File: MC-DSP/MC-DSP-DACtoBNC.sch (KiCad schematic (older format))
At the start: 1 part

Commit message: ADC refs, FTDI changes, and more
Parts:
- removed J?: Conn_Coaxial, symbol Connector:Conn_Coaxial
- added C? (x3): 0.1uF, symbol Device:C
- added J?: CONMMCX001, LINX_CONMMCX001, symbol CONMMCX001:CONMMCX001
- added R? (x2): ?R, symbol Device:R
- added R?: 0R, symbol Device:R
- added U?: OPA365xxD, Package_SO:SOIC-8_3.9x4.9mm_P1.27mm, symbol Amplifier_Operational:OPA365xxD
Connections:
- net labels added: DAC_A, DAC_B, DAC_C, VDDA
- net labels removed: DACfromDSP
- wire segments 1 -> 17
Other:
- note added: "check datasheet to pick between VDDA (3.3V) or VDAC (3V)"
- note added: "note offset error of 1-15 mV\n"
- note added: "read Output Capacitive Loading and Stability\n, add pads for an input resistor"
- note added: "verify input range\n"
- note removed: "Look for line driver amplifiers (look at appnotes)"
- note removed: "switch to mmcx"
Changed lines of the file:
@@
 $Descr A4 11693 8268
 encoding utf-8
-Sheet 9 9
+Sheet 7 9
 Title ""
 Date ""
@@
 Comment4 ""
 $EndDescr
-$Comp
-L Connector:Conn_Coaxial J?
-U 1 1 61B9DADA
-P 7400 2700
-F 0 "J?" H 7500 2675 50  0000 L CNN
-F 1 "Conn_Coaxial" H 7500 2584 50  0000 L CNN
-F 2 "" H 7400 2700 50  0001 C CNN
-F 3 " ~" H 7400 2700 50  0001 C CNN
-	1    7400 2700
-	1    0    0    -1
-$EndComp
-Text HLabel 4450 2650 0    50   Input ~ 0
-DACfromDSP
+Text HLabel 4600 2850 0    50   Input ~ 0
+DAC_A
 $Comp
 L power:GND #PWR?
 U 1 1 61B9E54E
-P 7400 3150
-F 0 "#PWR?" H 7400 2900 50  0001 C CNN
-F 1 "GND" H 7405 2977 50  0000 C CNN
-F 2 "" H 7400 3150 50  0001 C CNN
-F 3 "" H 7400 3150 50  0001 C CNN
-	1    7400 3150
-	1    0    0    -1
-$EndComp
-Wire Wire Line
-	7400 3150 7400 2900
-Text Notes 4950 2400 0    50   ~ 0
-Look for line driver amplifiers (look at appnotes)
-Text Notes 7450 2450 0    50   ~ 0
-switch to mmcx
+P 7350 3300
+F 0 "#PWR?" H 7350 3050 50  0001 C CNN
+F 1 "GND" H 7355 3127 50  0000 C CNN
+F 2 "" H 7350 3300 50  0001 C CNN
+F 3 "" H 7350 3300 50  0001 C CNN
+	1    7350 3300
+	1    0    0    -1
+$EndComp
+Wire Wire Line
+	7350 3300 7350 3050
+Wire Wire Line
+	6250 2950 6350 2950
+Wire Wire Line
+	5650 2850 5300 2850
+$Comp
+L CONMMCX001:CONMMCX001 J?
+U 1 1 61F03ABB
+P 7450 3050
+F 0 "J?" H 7296 3136 50  0000 R CNN
+F 1 "CONMMCX001" H 7296 3045 50  0000 R CNN
+F 2 "LINX_CONMMCX001" H 7450 3050 50  0001 L BNN
+F 3 "" H 7450 3050 50  0001 L BNN
+F 4 "B" H 7450 3050 50  0001 L BNN "PARTREV"
+F 5 "Manufacturer Recommendations" H 7450 3050 50  0001 L BNN "STANDARD"
+F 6 "Linx Technologies" H 7450 3050 50  0001 L BNN "MANUFACTURER"
+	1    7450 3050
+	-1   0    0    -1
+$EndComp
+Text HLabel 4450 3900 0    50   Input ~ 0
+DAC_B
+Text HLabel 4450 4750 0    50   Input ~ 0
+DAC_C
+Text Notes 6500 1100 0    50   ~ 0
+verify input range\n
+Text Notes 6400 1200 0    50   ~ 0
+note offset error of 1-15 mV\n
+Text Notes 7550 1050 0    50   ~ 0
+read Output Capacitive Loading and Stability\n, add pads for an input resistor
+$Comp
+L Amplifier_Operational:OPA365xxD U?
+U 1 1 622D9ECC
+P 5950 2950
+F 0 "U?" H 5950 3200 50  0000 L CNN
+F 1 "OPA365xxD" H 5950 3100 50  0000 L CNN
+F 2 "Package_SO:SOIC-8_3.9x4.9mm_P1.27mm" H 5850 2750 50  0001 L CNN
+F 3 "http://www.ti.com/lit/ds/symlink/opa365.pdf" H 6100 3100 50  0001 C CNN
+	1    5950 2950
+	1    0    0    -1
+$EndComp
+$Comp
+L power:GND #PWR?
+U 1 1 62433A6D
+P 3950 2050
+AR Path="/62086B6E/62433A6D" Ref="#PWR?"  Part="1"
+AR Path="/61B9C0F2/62433A6D" Ref="#PWR?"  Part="1"
+F 0 "#PWR?" H 3950 1800 50  0001 C CNN
+F 1 "GND" H 3955 1877 50  0000 C CNN
+F 2 "" H 3950 2050 50  0001 C CNN
+F 3 "" H 3950 2050 50  0001 C CNN
+	1    3950 2050
+	1    0    0    -1
+$EndComp
+$Comp
+L Device:C C?
+U 1 1 62433A73
+P 3800 1900
+F 0 "C?" H 3750 1800 50  0000 R CNN
+F 1 "0.1uF" H 3750 2000 50  0000 R CNN
+F 2 "" H 3838 1750 50  0001 C CNN
+F 3 "~" H 3800 1900 50  0001 C CNN
+	1    3800 1900
+	-1   0    0    1
+$EndComp
+$Comp
+L power:VDDA #PWR?
+U 1 1 62433A79
+P 3950 1750
+AR Path="/62086B6E/62433A79" Ref="#PWR?"  Part="1"
+AR Path="/61B9C0F2/62433A79" Ref="#PWR?"  Part="1"
+F 0 "#PWR?" H 3950 1600 50  0001 C CNN
+F 1 "VDDA" H 3965 1923 50  0000 C CNN
+F 2 "" H 3950 1750 50  0001 C CNN
+F 3 "" H 3950 1750 50  0001 C CNN
+	1    3950 1750
+	1    0    0    -1
+$EndComp
+$Comp
+L Device:C C?
+U 1 1 62433A7F
+P 4100 1900
+F 0 "C?" H 4050 1800 50  0000 R CNN
+F 1 "0.1uF" H 4050 2000 50  0000 R CNN
+F 2 "" H 4138 1750 50  0001 C CNN
+F 3 "~" H 4100 1900 50  0001 C CNN
+	1    4100 1900
+	-1   0    0    1
+$EndComp
+$Comp
+L Device:C C?
+U 1 1 62433A85
+P 4400 1900
+F 0 "C?" H 4350 1800 50  0000 R CNN
+F 1 "0.1uF" H 4350 2000 50  0000 R CNN
+F 2 "" H 4438 1750 50  0001 C CNN
+F 3 "~" H 4400 1900 50  0001 C CNN
+	1    4400 1900
+	-1   0    0    1
+$EndComp
+Wire Wire Line
+	3950 1750 3800 1750
+Connection ~ 4100 1750
+Wire Wire Line
+	4100 1750 4400 1750
+Wire Wire Line
+	3800 2050 3950 2050
+Connection ~ 4100 2050
+Wire Wire Line
+	4100 2050 4400 2050
+Connection ~ 3950 1750
+Wire Wire Line
+	3950 1750 4100 1750
+Connection ~ 3950 2050
+Wire Wire Line
+	3950 2050 4100 2050
+$Comp
+L power:VDDA #PWR?
+U 1 1 624345BF
+P 5850 2650
+AR Path="/62086B6E/624345BF" Ref="#PWR?"  Part="1"
+AR Path="/61B9C0F2/624345BF" Ref="#PWR?"  Part="1"
+F 0 "#PWR?" H 5850 2500 50  0001 C CNN
+F 1 "VDDA" H 6000 2700 50  0000 C CNN
+F 2 "" H 5850 2650 50  0001 C CNN
+F 3 "" H 5850 2650 50  0001 C CNN
+	1    5850 2650
+	1    0    0    -1
+$EndComp
+$Comp
+L power:GND #PWR?
+U 1 1 6243580E
+P 5850 3250
+AR Path="/62086B6E/6243580E" Ref="#PWR?"  Part="1"
+AR Path="/61B9C0F2/6243580E" Ref="#PWR?"  Part="1"
+F 0 "#PWR?" H 5850 3000 50  0001 C CNN
+F 1 "GND" H 6000 3200 50  0000 C CNN
+F 2 "" H 5850 3250 50  0001 C CNN
+F 3 "" H 5850 3250 50  0001 C CNN
+	1    5850 3250
+	1    0    0    -1
+$EndComp
+Wire Wire Line
+	5650 3050 5550 3050
+Wire Wire Line
+	5550 3050 5550 3450
+Wire Wire Line
+	5550 3450 5750 3450
+Wire Wire Line
+	6350 3450 6350 2950
+Connection ~ 6350 2950
+Wire Wire Line
+	6350 2950 6700 2950
+$Comp
+L Device:R R?
+U 1 1 62439A67
+P 6850 2950
+F 0 "R?" V 6850 2950 50  0000 C CNN
+F 1 "?R" V 6734 2950 50  0000 C CNN
+F 2 "" V 6780 2950 50  0001 C CNN
+F 3 "~" H 6850 2950 50  0001 C CNN
+	1    6850 2950
+	0    1    1    0
+$EndComp
+Wire Wire Line
+	7000 2950 7350 2950
+$Comp
+L Device:R R?
+U 1 1 6243BA69
+P 5150 2850
+F 0 "R?" V 5150 2850 50  0000 C CNN
+F 1 "0R" V 5034 2850 50  0000 C CNN
+F 2 "" V 5080 2850 50  0001 C CNN
+F 3 "~" H 5150 2850 50  0001 C CNN
+	1    5150 2850
+	0    1    1    0
+$EndComp
+Wire Wire Line
+	5000 2850 4600 2850
+$Comp
+L Device:R R?
+U 1 1 6243CB15
+P 5900 3450
+F 0 "R?" V 5900 3450 50  0000 C CNN
+F 1 "?R" V 6000 3450 50  0000 C CNN
+F 2 "" V 5830 3450 50  0001 C CNN
+F 3 "~" H 5900 3450 50  0001 C CNN
+	1    5900 3450
+	0    1    1    0
+$EndComp
+Wire Wire Line
+	6050 3450 6350 3450
+Text Notes 5600 2450 0    50   ~ 0
+check datasheet to pick between VDDA (3.3V) or VDAC (3V)
 $EndSCHEMATC

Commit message: fixed some dsp pin routing
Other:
- note removed: "check datasheet to pick between VDDA (3.3V) or VDAC (3V)"
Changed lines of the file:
@@
 Wire Wire Line
 	6050 3450 6350 3450
-Text Notes 5600 2450 0    50   ~ 0
-check datasheet to pick between VDDA (3.3V) or VDAC (3V)
 $EndSCHEMATC

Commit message: All parts labeled, just need to pick passives basically.
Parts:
- removed J?: CONMMCX001, LINX_CONMMCX001, symbol CONMMCX001:CONMMCX001
- added J60, J61, J62: Conn_Coaxial, ?, symbol Connector:Conn_Coaxial
- added R61, R62: 10R, Resistor_SMD:R_0603_1608Metric_Pad0.98x0.95mm_HandSolder, symbol Device:R
- added R64, R65, R67, R68: 0R, Resistor_SMD:R_0603_1608Metric_Pad0.98x0.95mm_HandSolder, symbol Device:R
- added U61, U62: OPA365xxD, Package_SO:SOIC-8_3.9x4.9mm_P1.27mm, symbol Amplifier_Operational:OPA365xxD
- C60, C61, C62: renamed from C?; footprint (none) -> Capacitor_SMD:C_0201_0603Metric_Pad0.64x0.40mm_HandSolder
- R60: renamed from R?; value ?R -> 10R; footprint (none) -> Resistor_SMD:R_0603_1608Metric_Pad0.98x0.95mm_HandSolder
- R63: renamed from R?; value ?R -> 0R; footprint (none) -> Resistor_SMD:R_0603_1608Metric_Pad0.98x0.95mm_HandSolder
- R66: renamed from R?; footprint (none) -> Resistor_SMD:R_0603_1608Metric_Pad0.98x0.95mm_HandSolder
- gave numbers to parts that had none: 1
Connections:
- wire segments 17 -> 39
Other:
- note removed: "note offset error of 1-15 mV\n"
- note removed: "read Output Capacitive Loading and Stability\n, add pads for an input resistor"
- note removed: "verify input range\n"
- moved on the sheet: C60, C61, C62

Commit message: DSP - added footprints and links to most parts
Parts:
- removed J60, J61, J62: Conn_Coaxial, ?, symbol Connector:Conn_Coaxial
- added J80, J81, J82: 5-1634513-1, 516345131, symbol 5-1634513-1:5-1634513-1
- renumbered C60 to C80, C61 to C81, C62 to C82, R60 to R80, R61 to R81, R62 to R82, R63 to R83, R64 to R84, R65 to R85, R66 to R86, R67 to R87, R68 to R88, U60 to U80, U61 to U81, U62 to U82
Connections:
- wire segments 39 -> 54

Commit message: Removed clock buffer, misc leds, ethernet
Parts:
- C80, C81, C82: footprint Capacitor_SMD:C_0201_0603Metric_Pad0.64x0.40mm_HandSolder -> Capacitor_SMD:C_0603_1608Metric_Pad1.08x0.95mm_HandSolder
- J80, J81, J82: footprint 516345131 -> mark_footprints:516345131
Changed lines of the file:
@@
 $Descr A4 11693 8268
 encoding utf-8
-Sheet 7 9
+Sheet 7 7
 Title ""
 Date ""
@@
 F 0 "C80" H 4600 1850 50  0000 R CNN
 F 1 "0.1uF" H 4600 2050 50  0000 R CNN
-F 2 "Capacitor_SMD:C_0201_0603Metric_Pad0.64x0.40mm_HandSolder" H 4688 1800 50  0001 C CNN
+F 2 "Capacitor_SMD:C_0603_1608Metric_Pad1.08x0.95mm_HandSolder" H 4688 1800 50  0001 C CNN
 F 3 "https://www.digikey.com/en/products/detail/yageo/CC0603KRX7R9BB104/2103082" H 4650 1950 50  0001 C CNN
 	1    4650 1950
@@
 F 0 "C81" H 4900 1850 50  0000 R CNN
 F 1 "0.1uF" H 4900 2050 50  0000 R CNN
-F 2 "Capacitor_SMD:C_0201_0603Metric_Pad0.64x0.40mm_HandSolder" H 4988 1800 50  0001 C CNN
+F 2 "Capacitor_SMD:C_0603_1608Metric_Pad1.08x0.95mm_HandSolder" H 4988 1800 50  0001 C CNN
 F 3 "https://www.digikey.com/en/products/detail/yageo/CC0603KRX7R9BB104/2103082" H 4950 1950 50  0001 C CNN
 	1    4950 1950
@@
 F 0 "C82" H 5200 1850 50  0000 R CNN
 F 1 "0.1uF" H 5200 2050 50  0000 R CNN
-F 2 "Capacitor_SMD:C_0201_0603Metric_Pad0.64x0.40mm_HandSolder" H 5288 1800 50  0001 C CNN
+F 2 "Capacitor_SMD:C_0603_1608Metric_Pad1.08x0.95mm_HandSolder" H 5288 1800 50  0001 C CNN
 F 3 "https://www.digikey.com/en/products/detail/yageo/CC0603KRX7R9BB104/2103082" H 5250 1950 50  0001 C CNN
 	1    5250 1950
@@
 F 0 "J80" H 7750 3215 50  0000 C CNN
 F 1 "5-1634513-1" H 7750 3124 50  0000 C CNN
-F 2 "516345131" H 8000 3050 50  0001 L CNN
+F 2 "mark_footprints:516345131" H 8000 3050 50  0001 L CNN
 F 3 "https://www.digikey.com/en/products/detail/te-connectivity-amp-connectors/5-1634513-1/1755956?s=N4IgTCBcDaIKwFoCMA2AzAFjktyQF0BfIA" H 8000 2950 50  0001 L CNN
 F 4 "Connector,Coaxial,BNC,PCB,Socket,R/A,Elbow,50Ohm,Nickel Plated,28.0mm" H 8000 2850 50  0001 L CNN "Description"
@@
 F 0 "J81" H 7750 4515 50  0000 C CNN
 F 1 "5-1634513-1" H 7750 4424 50  0000 C CNN
-F 2 "516345131" H 8000 4350 50  0001 L CNN
+F 2 "mark_footprints:516345131" H 8000 4350 50  0001 L CNN
 F 3 "https://www.digikey.com/en/products/detail/te-connectivity-amp-connectors/5-1634513-1/1755956?s=N4IgTCBcDaIKwFoCMA2AzAFjktyQF0BfIA" H 8000 4250 50  0001 L CNN
 F 4 "Connector,Coaxial,BNC,PCB,Socket,R/A,Elbow,50Ohm,Nickel Plated,28.0mm" H 8000 4150 50  0001 L CNN "Description"
@@
 F 0 "J82" H 7750 5715 50  0000 C CNN
 F 1 "5-1634513-1" H 7750 5624 50  0000 C CNN
-F 2 "516345131" H 8000 5550 50  0001 L CNN
+F 2 "mark_footprints:516345131" H 8000 5550 50  0001 L CNN
 F 3 "https://www.digikey.com/en/products/detail/te-connectivity-amp-connectors/5-1634513-1/1755956?s=N4IgTCBcDaIKwFoCMA2AzAFjktyQF0BfIA" H 8000 5450 50  0001 L CNN
 F 4 "Connector,Coaxial,BNC,PCB,Socket,R/A,Elbow,50Ohm,Nickel Plated,28.0mm" H 8000 5350 50  0001 L CNN "Description"

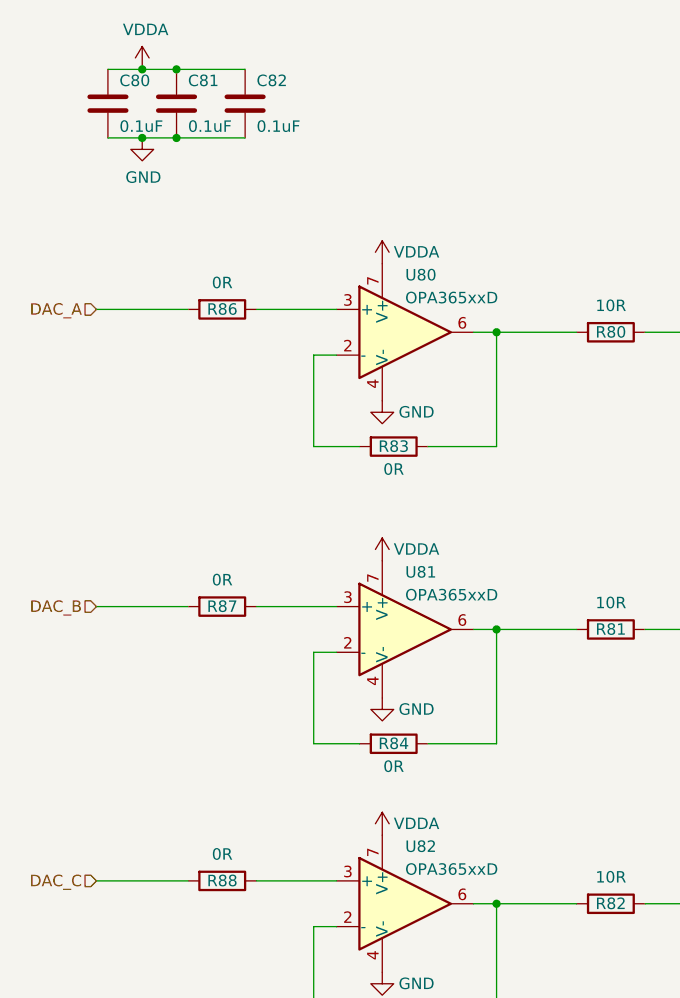
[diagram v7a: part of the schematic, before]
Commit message: Total overhaul of power planes. Routed whole Analog section, middle of digital section.
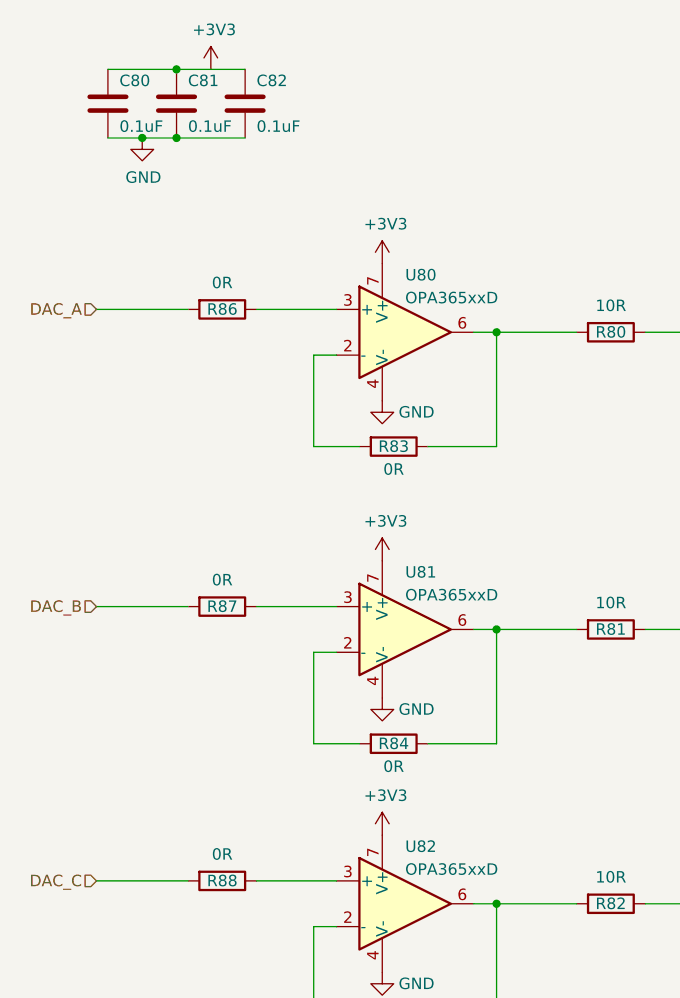
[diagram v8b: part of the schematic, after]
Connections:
- net VDDA: no longer names the net of C80.2, C81.2, C82.2
- net VDDA: no longer U80.7 (V+), U81.7 (V+), U82.7 (V+)
- new net +3V3: U80.7 (V+), U81.7 (V+), U82.7 (V+)
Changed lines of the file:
@@
 $Descr A4 11693 8268
 encoding utf-8
-Sheet 4 7
+Sheet 2 7
 Title ""
 Date ""
@@
 $EndComp
 $Comp
-L power:VDDA #PWR?
-U 1 1 62433A79
-P 4800 1800
-AR Path="/62086B6E/62433A79" Ref="#PWR?"  Part="1"
-AR Path="/61B9C0F2/62433A79" Ref="#PWR0173"  Part="1"
-F 0 "#PWR0173" H 4800 1650 50  0001 C CNN
-F 1 "VDDA" H 4815 1973 50  0000 C CNN
-F 2 "" H 4800 1800 50  0001 C CNN
-F 3 "" H 4800 1800 50  0001 C CNN
-	1    4800 1800
-	1    0    0    -1
-$EndComp
-$Comp
 L Device:C C81
 U 1 1 62433A7F
@@
 	-1   0    0    1
 $EndComp
-Wire Wire Line
-	4800 1800 4650 1800
 Connection ~ 4950 1800
 Wire Wire Line
@@
 Wire Wire Line
 	4950 2100 5250 2100
-Connection ~ 4800 1800
-Wire Wire Line
-	4800 1800 4950 1800
 Connection ~ 4800 2100
 Wire Wire Line
 	4800 2100 4950 2100
-$Comp
-L power:VDDA #PWR?
-U 1 1 624345BF
-P 5850 2650
-AR Path="/62086B6E/624345BF" Ref="#PWR?"  Part="1"
-AR Path="/61B9C0F2/624345BF" Ref="#PWR0174"  Part="1"
-F 0 "#PWR0174" H 5850 2500 50  0001 C CNN
-F 1 "VDDA" H 6000 2700 50  0000 C CNN
-F 2 "" H 5850 2650 50  0001 C CNN
-F 3 "" H 5850 2650 50  0001 C CNN
-	1    5850 2650
-	1    0    0    -1
-$EndComp
 $Comp
 L power:GND #PWR?
@@
 $EndComp
 $Comp
-L power:VDDA #PWR?
-U 1 1 6337731D
-P 5850 3950
-AR Path="/62086B6E/6337731D" Ref="#PWR?"  Part="1"
-AR Path="/61B9C0F2/6337731D" Ref="#PWR0176"  Part="1"
-F 0 "#PWR0176" H 5850 3800 50  0001 C CNN
-F 1 "VDDA" H 6000 4000 50  0000 C CNN
-F 2 "" H 5850 3950 50  0001 C CNN
-F 3 "" H 5850 3950 50  0001 C CNN
-	1    5850 3950
-	1    0    0    -1
-$EndComp
-$Comp
 L power:GND #PWR?
 U 1 1 63377323
@@
 F 3 "https://www.digikey.com/en/products/detail/texas-instruments/OPA365AID/1219893" H 6100 5600 50  0001 C CNN
 	1    5950 5450
-	1    0    0    -1
-$EndComp
-$Comp
-L power:VDDA #PWR?
-U 1 1 6337C61B
-P 5850 5150
-AR Path="/62086B6E/6337C61B" Ref="#PWR?"  Part="1"
-AR Path="/61B9C0F2/6337C61B" Ref="#PWR0178"  Part="1"
-F 0 "#PWR0178" H 5850 5000 50  0001 C CNN
-F 1 "VDDA" H 6000 5200 50  0000 C CNN
-F 2 "" H 5850 5150 50  0001 C CNN
-F 3 "" H 5850 5150 50  0001 C CNN
-	1    5850 5150
 	1    0    0    -1
 $EndComp
@@
 Wire Wire Line
 	7350 4250 7000 4250
+$Comp
+L power:+3V3 #PWR?
+U 1 1 6242ED79
+P 5850 3950
+AR Path="/6187F723/6242ED79" Ref="#PWR?"  Part="1"
+AR Path="/61B9C0F2/6242ED79" Ref="#PWR0139"  Part="1"
+F 0 "#PWR0139" H 5850 3800 50  0001 C CNN
+F 1 "+3V3" H 5865 4123 50  0000 C CNN
+F 2 "" H 5850 3950 50  0001 C CNN
+F 3 "" H 5850 3950 50  0001 C CNN
+	1    5850 3950
+	1    0    0    -1
+$EndComp
+$Comp
+L power:+3V3 #PWR?
+U 1 1 62430BBE
+P 5850 2650
+AR Path="/6187F723/62430BBE" Ref="#PWR?"  Part="1"
+AR Path="/61B9C0F2/62430BBE" Ref="#PWR0140"  Part="1"
+F 0 "#PWR0140" H 5850 2500 50  0001 C CNN
+F 1 "+3V3" H 5865 2823 50  0000 C CNN
+F 2 "" H 5850 2650 50  0001 C CNN
+F 3 "" H 5850 2650 50  0001 C CNN
+	1    5850 2650
+	1    0    0    -1
+$EndComp
+$Comp
+L power:+3V3 #PWR?
+U 1 1 62431898
+P 5850 5150
+AR Path="/6187F723/62431898" Ref="#PWR?"  Part="1"
+AR Path="/61B9C0F2/62431898" Ref="#PWR0141"  Part="1"
+F 0 "#PWR0141" H 5850 5000 50  0001 C CNN
+F 1 "+3V3" H 5865 5323 50  0000 C CNN
+F 2 "" H 5850 5150 50  0001 C CNN
+F 3 "" H 5850 5150 50  0001 C CNN
+	1    5850 5150
+	1    0    0    -1
+$EndComp
+$Comp
+L power:+3V3 #PWR?
+U 1 1 6243256E
+P 5100 1800
+AR Path="/6187F723/6243256E" Ref="#PWR?"  Part="1"
+AR Path="/61B9C0F2/6243256E" Ref="#PWR0142"  Part="1"
+F 0 "#PWR0142" H 5100 1650 50  0001 C CNN
+F 1 "+3V3" H 5115 1973 50  0000 C CNN
+F 2 "" H 5100 1800 50  0001 C CNN
+F 3 "" H 5100 1800 50  0001 C CNN
+	1    5100 1800
+	1    0    0    -1
+$EndComp
+Wire Wire Line
+	4650 1800 4950 1800
 $EndSCHEMATC
